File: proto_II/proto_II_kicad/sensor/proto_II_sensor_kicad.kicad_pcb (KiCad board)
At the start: 2 copper layers, 29 x 11 mm, 17 parts, among them J1 Conn_01x02, J2 Conn_01x02, U1 XC6206P332MR, U2 BME280, U3 Si7020-A20

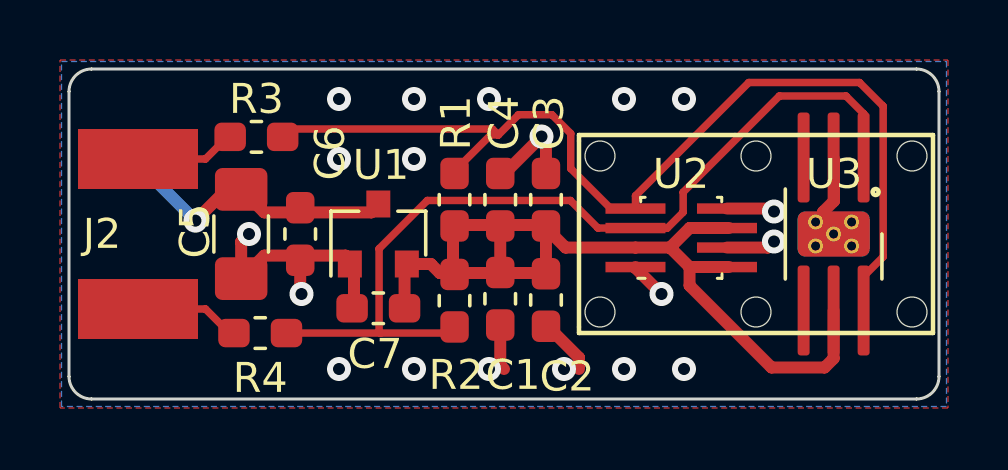
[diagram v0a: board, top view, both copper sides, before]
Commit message: Better field naming for components
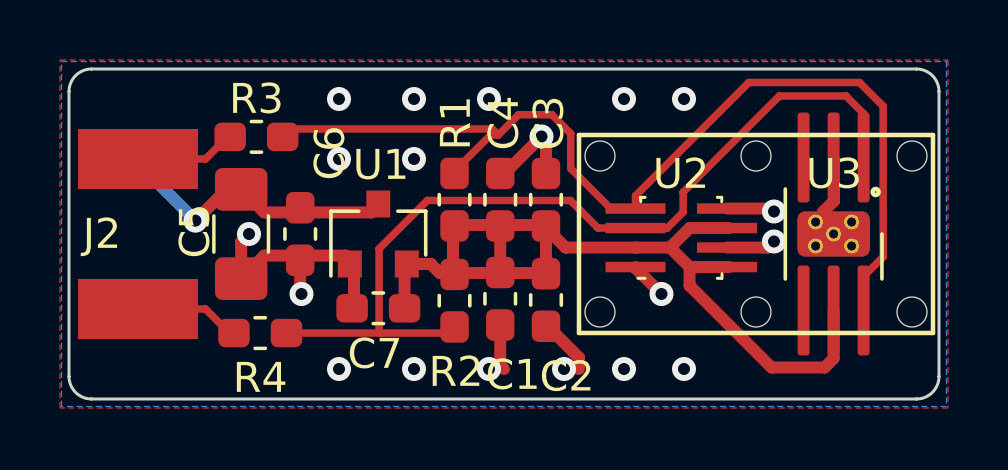
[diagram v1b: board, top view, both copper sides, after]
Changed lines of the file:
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@@
-(kicad_pcb (version 20190605) (host pcbnew "(5.1.0-1220-ga833aeeac)")
+(kicad_pcb (version 20171130) (host pcbnew 5.1.4)
   (general
     (thickness 1.5)
@@
   )
   (setup
-    (last_trace_width 0.4)
+    (last_trace_width 0.25)
     (user_trace_width 0.4)
     (trace_clearance 0.2)
@@
     (uvia_min_size 0.2)
     (uvia_min_drill 0.1)
-    (max_error 0.005)
-    (defaults
-      (edge_clearance 0.01)
-      (edge_cuts_line_width 0.1)
-      (courtyard_line_width 0.05)
-      (copper_line_width 0.2)
-      (copper_text_dims (size 1.5 1.5) (thickness 0.3) keep_upright)
-      (silk_line_width 0.15)
-      (silk_text_dims (size 1 1) (thickness 0.15) keep_upright)
-      (other_layers_line_width 0.1)
-      (other_layers_text_dims (size 1 1) (thickness 0.15) keep_upright)
-    )
     (pad_size 1 1)
     (pad_drill 1)
@@
     (add_net "/SDA_IC")
     (add_net "GND")
+  )
+  (module "Project:Bosch_LGA-8_2.5x2.5mm_P0.65mm_ClockwisePinNumbering_HandSoldering" (layer "F.Cu")
+    (at 55.9075 28.377 90)
+    (descr "LGA-8")
+    (tags "lga land grid array")
+    (attr smd)
+    (fp_text reference "U2" (at 2.127 -0.0075 180) (layer "F.SilkS")
+      (effects (font (size 1 1) (thickness 0.15)))
+    )
+    (fp_text value "BME280" (at 0.015 3.585 90) (layer "F.Fab")
+      (effects (font (size 1 1) (thickness 0.15)))
+    )
+    (fp_text user "%R" (at 0 0 270) (layer "F.Fab")
+      (effects (font (size 0.5 0.5) (thickness 0.075)))
+    )
+    (fp_line (start -1.35 1.36) (end -1.2 1.36) (layer "F.SilkS") (width 0.1))
+    (fp_line (start -1.25 -0.5) (end -0.5 -1.25) (layer "F.Fab") (width 0.1))
+    (fp_line (start -1.35 1.35) (end -1.35 1.2) (layer "F.SilkS") (width 0.1))
+    (fp_line (start 1.35 1.35) (end 1.35 1.2) (layer "F.SilkS") (width 0.1))
+    (fp_line (start 1.35 1.35) (end 1.2 1.35) (layer "F.SilkS") (width 0.1))
+    (fp_line (start 1.2 -1.35) (end 1.35 -1.35) (layer "F.SilkS") (width 0.1))
+    (fp_line (start 1.35 -1.35) (end 1.35 -1.2) (layer "F.SilkS") (width 0.1))
+    (fp_line (start -1.35 -1.2) (end -1.35 -1.45) (layer "F.SilkS") (width 0.1))
+    (fp_line (start -1.25 1.25) (end -1.25 -0.5) (layer "F.Fab") (width 0.1))
+    (fp_line (start -0.5 -1.25) (end 1.25 -1.25) (layer "F.Fab") (width 0.1))
+    (fp_line (start 1.25 -1.25) (end 1.25 1.25) (layer "F.Fab") (width 0.1))
+    (fp_line (start 1.25 1.25) (end -1.25 1.25) (layer "F.Fab") (width 0.1))
+    (fp_line (start -1.41 2.59) (end -1.41 -2.59) (layer "F.CrtYd") (width 0.05))
+    (fp_line (start -1.41 -2.59) (end 1.41 -2.59) (layer "F.CrtYd") (width 0.05))
+    (fp_line (start 1.41 -2.59) (end 1.41 2.59) (layer "F.CrtYd") (width 0.05))
+    (fp_line (start 1.41 2.59) (end -1.41 2.59) (layer "F.CrtYd") (width 0.05))
+    (pad "4" smd rect (at 0.975 -1.525 180) (size 2 0.35) (layers "F.Cu" "F.Paste" "F.Mask")
+      (net 6 "/SCL_IC"))
+    (pad "3" smd rect (at 0.325 -1.525 180) (size 2 0.35) (layers "F.Cu" "F.Paste" "F.Mask")
+      (net 7 "/SDA_IC"))
+    (pad "2" smd rect (at -0.325 -1.525 180) (size 2 0.35) (layers "F.Cu" "F.Paste" "F.Mask")
+      (net 1 "+3V3"))
+    (pad "1" smd rect (at -0.975 -1.525 180) (size 2 0.35) (layers "F.Cu" "F.Paste" "F.Mask")
+      (net 2 "GND"))
+    (pad "8" smd rect (at -0.975 1.525 180) (size 2 0.35) (layers "F.Cu" "F.Paste" "F.Mask")
+      (net 1 "+3V3"))
+    (pad "7" smd rect (at -0.325 1.525 180) (size 2 0.35) (layers "F.Cu" "F.Paste" "F.Mask")
+      (net 2 "GND"))
+    (pad "6" smd rect (at 0.325 1.525 180) (size 2 0.35) (layers "F.Cu" "F.Paste" "F.Mask")
+      (net 1 "+3V3"))
+    (pad "5" smd rect (at 0.975 1.525 180) (size 2 0.35) (layers "F.Cu" "F.Paste" "F.Mask")
+      (net 2 "GND"))
+    (model "${KISYS3DMOD}/Package_LGA.3dshapes/Bosch_LGA-8_2.5x2.5mm_P0.65mm_ClockwisePinNumbering.wrl"
+      (offset (xyz 0.01500000025472259 -0.03500000059435272 0))
+      (scale (xyz 1 1 1))
+      (rotate (xyz 0 0 0))
+    )
   )
   (module "Project:SENSIRION-SF2-2PLACE" locked (layer "F.Cu")
@@
     )
   )
-  (module "Project:Bosch_LGA-8_2.5x2.5mm_P0.65mm_ClockwisePinNumbering_HandSoldering" (layer "F.Cu")
-    (at 55.9075 28.377 90)
-    (descr "LGA-8")
-    (tags "lga land grid array")
-    (attr smd)
-    (fp_text reference "U2" (at 2.127 -0.0075 180) (layer "F.SilkS")
-      (effects (font (size 1 1) (thickness 0.15)))
-    )
-    (fp_text value "BME280" (at 0.015 3.585 90) (layer "F.Fab")
-      (effects (font (size 1 1) (thickness 0.15)))
-    )
-    (fp_text user "%R" (at 0 0 270) (layer "F.Fab")
-      (effects (font (size 0.5 0.5) (thickness 0.075)))
-    )
-    (fp_line (start -1.35 1.36) (end -1.2 1.36) (layer "F.SilkS") (width 0.1))
-    (fp_line (start -1.25 -0.5) (end -0.5 -1.25) (layer "F.Fab") (width 0.1))
-    (fp_line (start -1.35 1.35) (end -1.35 1.2) (layer "F.SilkS") (width 0.1))
-    (fp_line (start 1.35 1.35) (end 1.35 1.2) (layer "F.SilkS") (width 0.1))
-    (fp_line (start 1.35 1.35) (end 1.2 1.35) (layer "F.SilkS") (width 0.1))
-    (fp_line (start 1.2 -1.35) (end 1.35 -1.35) (layer "F.SilkS") (width 0.1))
-    (fp_line (start 1.35 -1.35) (end 1.35 -1.2) (layer "F.SilkS") (width 0.1))
-    (fp_line (start -1.35 -1.2) (end -1.35 -1.45) (layer "F.SilkS") (width 0.1))
-    (fp_line (start -1.25 1.25) (end -1.25 -0.5) (layer "F.Fab") (width 0.1))
-    (fp_line (start -0.5 -1.25) (end 1.25 -1.25) (layer "F.Fab") (width 0.1))
-    (fp_line (start 1.25 -1.25) (end 1.25 1.25) (layer "F.Fab") (width 0.1))
-    (fp_line (start 1.25 1.25) (end -1.25 1.25) (layer "F.Fab") (width 0.1))
-    (fp_line (start -1.41 2.59) (end -1.41 -2.59) (layer "F.CrtYd") (width 0.05))
-    (fp_line (start -1.41 -2.59) (end 1.41 -2.59) (layer "F.CrtYd") (width 0.05))
-    (fp_line (start 1.41 -2.59) (end 1.41 2.59) (layer "F.CrtYd") (width 0.05))
-    (fp_line (start 1.41 2.59) (end -1.41 2.59) (layer "F.CrtYd") (width 0.05))
-    (pad "4" smd rect (at 0.975 -1.525 180) (size 2 0.35) (layers "F.Cu" "F.Paste" "F.Mask")
-      (net 6 "/SCL_IC"))
-    (pad "3" smd rect (at 0.325 -1.525 180) (size 2 0.35) (layers "F.Cu" "F.Paste" "F.Mask")
-      (net 7 "/SDA_IC"))
-    (pad "2" smd rect (at -0.325 -1.525 180) (size 2 0.35) (layers "F.Cu" "F.Paste" "F.Mask")
-      (net 1 "+3V3"))
-    (pad "1" smd rect (at -0.975 -1.525 180) (size 2 0.35) (layers "F.Cu" "F.Paste" "F.Mask")
-      (net 2 "GND"))
-    (pad "8" smd rect (at -0.975 1.525 180) (size 2 0.35) (layers "F.Cu" "F.Paste" "F.Mask")
-      (net 1 "+3V3"))
-    (pad "7" smd rect (at -0.325 1.525 180) (size 2 0.35) (layers "F.Cu" "F.Paste" "F.Mask")
-      (net 2 "GND"))
-    (pad "6" smd rect (at 0.325 1.525 180) (size 2 0.35) (layers "F.Cu" "F.Paste" "F.Mask")
-      (net 1 "+3V3"))
-    (pad "5" smd rect (at 0.975 1.525 180) (size 2 0.35) (layers "F.Cu" "F.Paste" "F.Mask")
-      (net 2 "GND"))
-    (model "${KISYS3DMOD}/Package_LGA.3dshapes/Bosch_LGA-8_2.5x2.5mm_P0.65mm_ClockwisePinNumbering.wrl"
-      (offset (xyz 0.01500000025472259 -0.03500000059435272 0))
-      (scale (xyz 1 1 1))
-      (rotate (xyz 0 0 0))
-    )
-  )
   (module "Package_TO_SOT_SMD:SOT-23" (layer "F.Cu")
     (at 45.811 28.25 90)
@@
     (tags "resistor handsolder")
     (attr smd)
-    (fp_text reference "R2" (at 2.4775 -0.049 180) (layer "F.SilkS")
+    (fp_text reference "R2" (at 2.3775 -0.049 180) (layer "F.SilkS")
       (effects (font (size 1 1) (thickness 0.15)))
     )
@@
     )
   )
+  (gr_line (start 66 28.25) (end 66 21.25) (layer "Eco1.User") (width 0.1))
+  (gr_line (start 66 28.25) (end 66 35.25) (layer "Eco1.User") (width 0.1))
+  (gr_line (start 66 21.25) (end 35 21.25) (layer "Eco1.User") (width 0.1))
+  (gr_line (start 35 21.25) (end 35 25) (layer "Eco1.User") (width 0.1))
+  (gr_line (start 66 35.25) (end 35 35.25) (layer "Eco1.User") (width 0.1))
+  (gr_line (start 35 31.5) (end 35 35.25) (layer "Eco1.User") (width 0.1))
   (gr_line (start 47.12591 28.06574) (end 46.844881 28.21613) (layer "B.SilkS") (width 0.1))
   (gr_line (start 49.99886 27.8682) (end 50.07741 27.8255) (layer "B.SilkS") (width 0.1))
@@
   (gr_line (start 64.5 33) (end 64.5 23.5) (layer "Edge.Cuts") (width 0.1))
   (gr_line (start 35 26.5) (end 35 30) (layer "Eco1.User") (width 0.1))
-  (gr_line (start 35 31.5) (end 35 35.25) (layer "Eco1.User") (width 0.1))
-  (gr_line (start 35 21.25) (end 35 25) (layer "Eco1.User") (width 0.1))
   (dimension 12 (width 0.1) (layer "Eco1.User")
     (gr_text "12.000 mm" (at 71 28.25 270) (layer "Eco1.User")
@@
   (gr_line (start 35 34.25) (end 65 34.25) (layer "Eco1.User") (width 0.1))
   (gr_line (start 65 34.25) (end 65 28.25) (layer "Eco1.User") (width 0.1))
-  (gr_line (start 66 28.25) (end 66 35.25) (layer "Eco1.User") (width 0.1))
-  (gr_line (start 66 35.25) (end 35 35.25) (layer "Eco1.User") (width 0.1))
-  (gr_line (start 66 21.25) (end 35 21.25) (layer "Eco1.User") (width 0.1))
-  (gr_line (start 66 28.25) (end 66 21.25) (layer "Eco1.User") (width 0.1))
   (gr_line (start 65 22.25) (end 65 28.25) (layer "Eco1.User") (width 0.1))
   (gr_line (start 35 22.25) (end 65 22.25) (layer "Eco1.User") (width 0.1))
@@
   (segment (start 37.8 25.75) (end 40.05 25.75) (width 0.25) (layer "F.Cu") (net 5))
   (segment (start 40.05 25.75) (end 40.731 25.069) (width 0.25) (layer "F.Cu") (net 5))
+  (zone (net 2) (net_name "GND") (layer "F.Cu") (hatch edge 0.508)
+    (connect_pads (clearance 0.508))
+    (min_thickness 0.254)
+    (fill yes (thermal_gap 0.508) (thermal_bridge_width 0.508))
+    (polygon
+      (pts
+        (xy 35.2 22.45) (xy 64.8 22.45) (xy 64.8 34.05) (xy 35.2 34.05)
+      )
+    )
+  )
   (zone (net 2) (net_name "GND") (layer "B.Cu") (hatch edge 0.508)
     (connect_pads (clearance 0.508))
@@
       )
     )
-  )
-  (zone (net 2) (net_name "GND") (layer "F.Cu") (hatch edge 0.508)
-    (connect_pads (clearance 0.508))
-    (min_thickness 0.254)
-    (fill yes (thermal_gap 0.508) (thermal_bridge_width 0.508))
-    (polygon
-      (pts
-        (xy 35.2 22.45) (xy 64.8 22.45) (xy 64.8 34.05) (xy 35.2 34.05)
-      )
-    )
